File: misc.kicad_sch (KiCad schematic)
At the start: 4 parts, among them J3 PinHeader_2x5_P1.27mm_SMD, U1 MPFS250T-FCVG484, U2 SDINBDG4-8G, U4 MT25QL01GBBB8E_SOP2-16

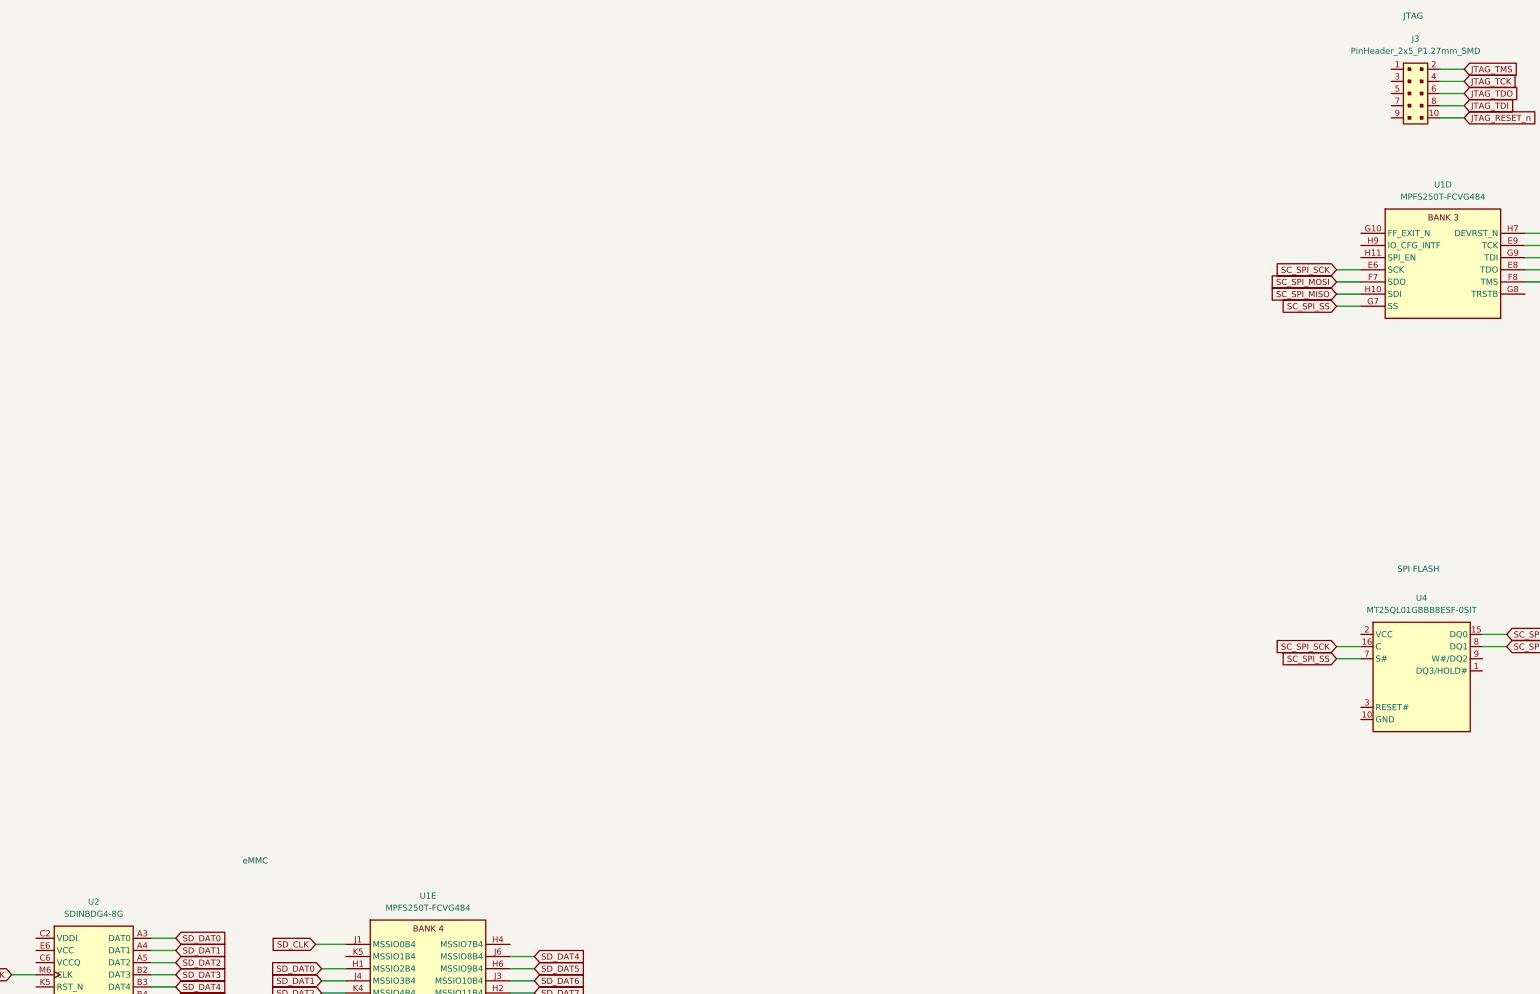
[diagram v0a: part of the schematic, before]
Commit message: [#52577] Clear annotations
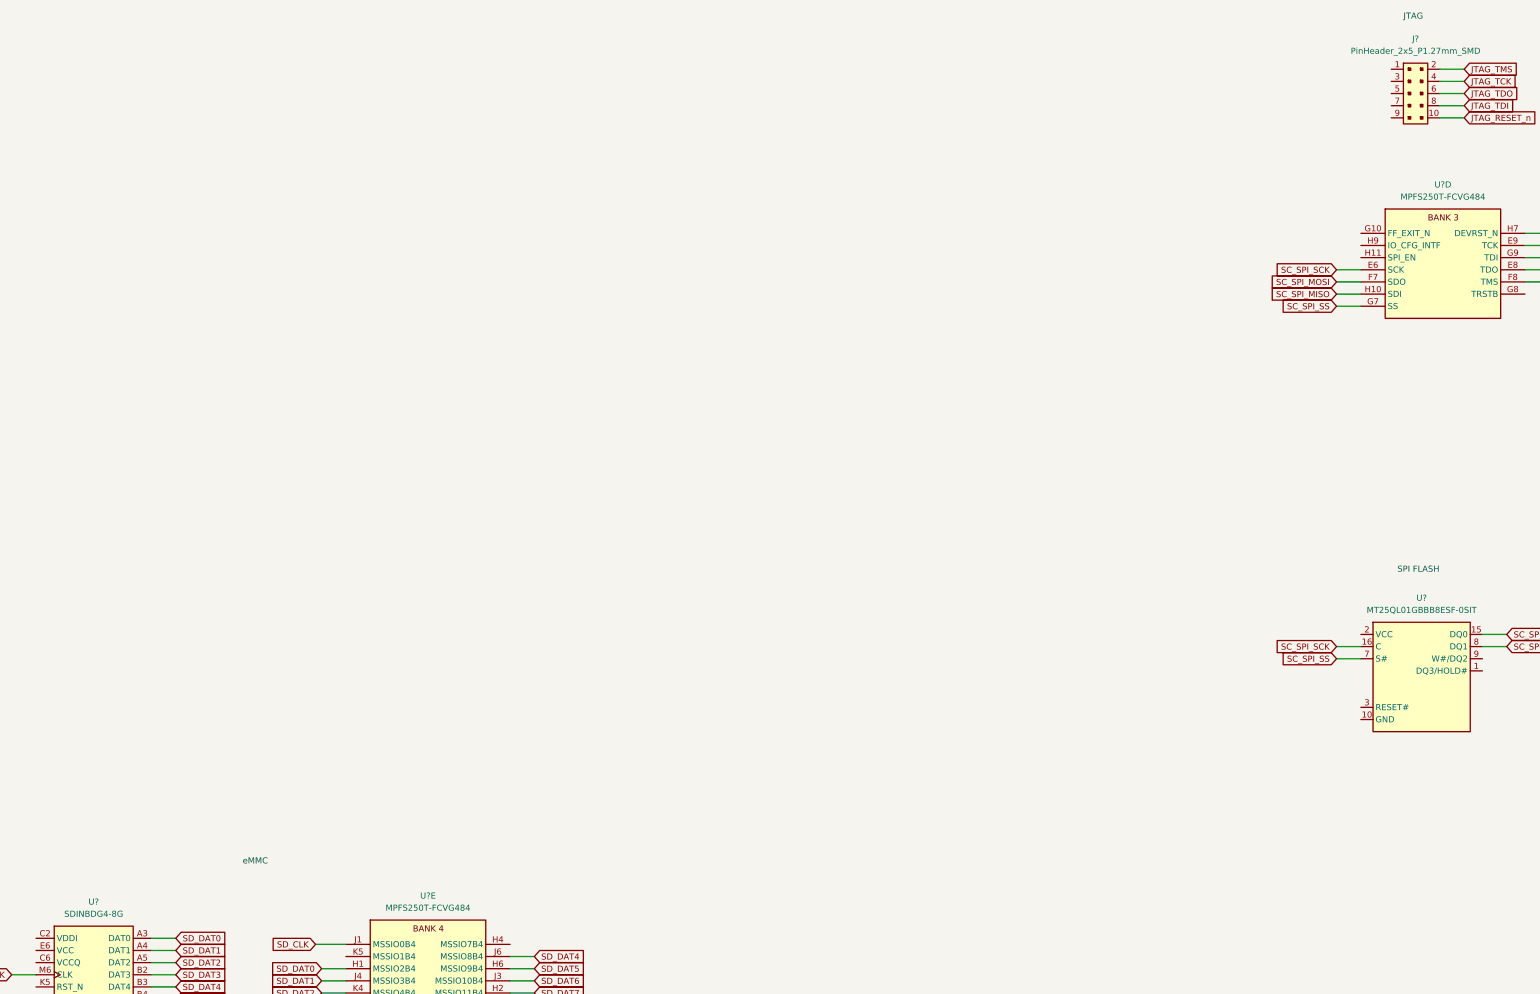
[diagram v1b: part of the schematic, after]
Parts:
- renumbered J3 to J?, U1 to U?, U2 to U?, U4 to U?
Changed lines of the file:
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@@
   (symbol (lib_id "antmicroMicrocontrollers:MPFS250T-FCVG484") (at 116.84 232.41 0) (unit 5)
     (in_bom yes) (on_board yes) (fields_autoplaced)
-    (property "Reference" "U1" (id 0) (at 133.985 222.25 0)
+    (property "Reference" "U?" (id 0) (at 133.985 222.25 0)
       (effects (font (size 1.27 1.27) (thickness 0.15)))
     )
@@
   (symbol (lib_id "antmicroMemory:SDINBDG4-8G") (at 52.07 231.14 0) (unit 1)
     (in_bom yes) (on_board yes) (fields_autoplaced)
-    (property "Reference" "U2" (id 0) (at 64.135 223.52 0)
+    (property "Reference" "U?" (id 0) (at 64.135 223.52 0)
       (effects (font (size 1.27 1.27) (thickness 0.15)))
     )
@@
   (symbol (lib_id "antmicroMemory:MT25QL01GBBB8E_SOP2-16") (at 326.39 167.64 0) (unit 1)
     (in_bom yes) (on_board yes) (fields_autoplaced)
-    (property "Reference" "U4" (id 0) (at 341.63 160.02 0)
+    (property "Reference" "U?" (id 0) (at 341.63 160.02 0)
       (effects (font (size 1.27 1.27) (thickness 0.15)))
     )
@@
   (symbol (lib_id "antmicroMicrocontrollers:MPFS250T-FCVG484") (at 328.93 83.82 0) (unit 4)
     (in_bom yes) (on_board yes) (fields_autoplaced)
-    (property "Reference" "U1" (id 0) (at 346.075 73.66 0)
+    (property "Reference" "U?" (id 0) (at 346.075 73.66 0)
       (effects (font (size 1.27 1.27) (thickness 0.15)))
     )
@@
   (symbol (lib_id "antmicroGenericPinHeaders:PinHeader_2x5_P1.27mm_SMD") (at 335.28 49.53 0) (unit 1)
     (in_bom yes) (on_board yes) (fields_autoplaced)
-    (property "Reference" "J3" (id 0) (at 340.36 43.18 0)
+    (property "Reference" "J?" (id 0) (at 340.36 43.18 0)
       (effects (font (size 1.27 1.27) (thickness 0.15)))
     )

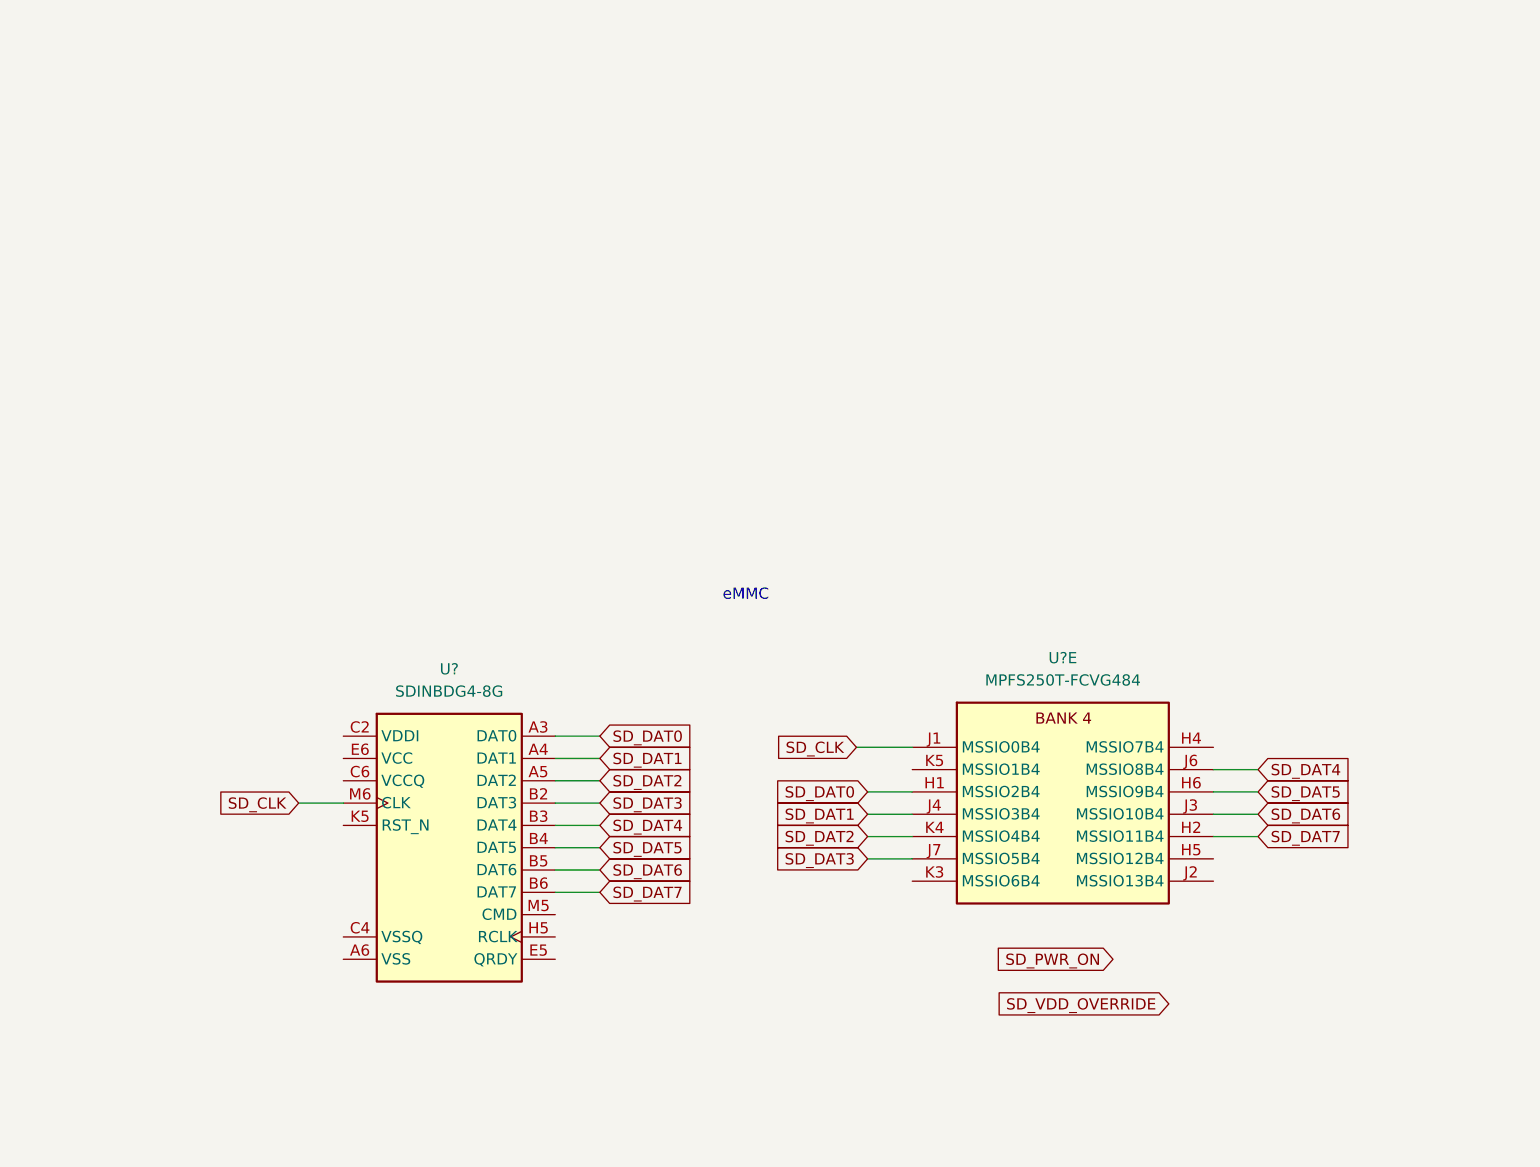
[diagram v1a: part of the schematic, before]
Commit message: [#54013] Add resistor array
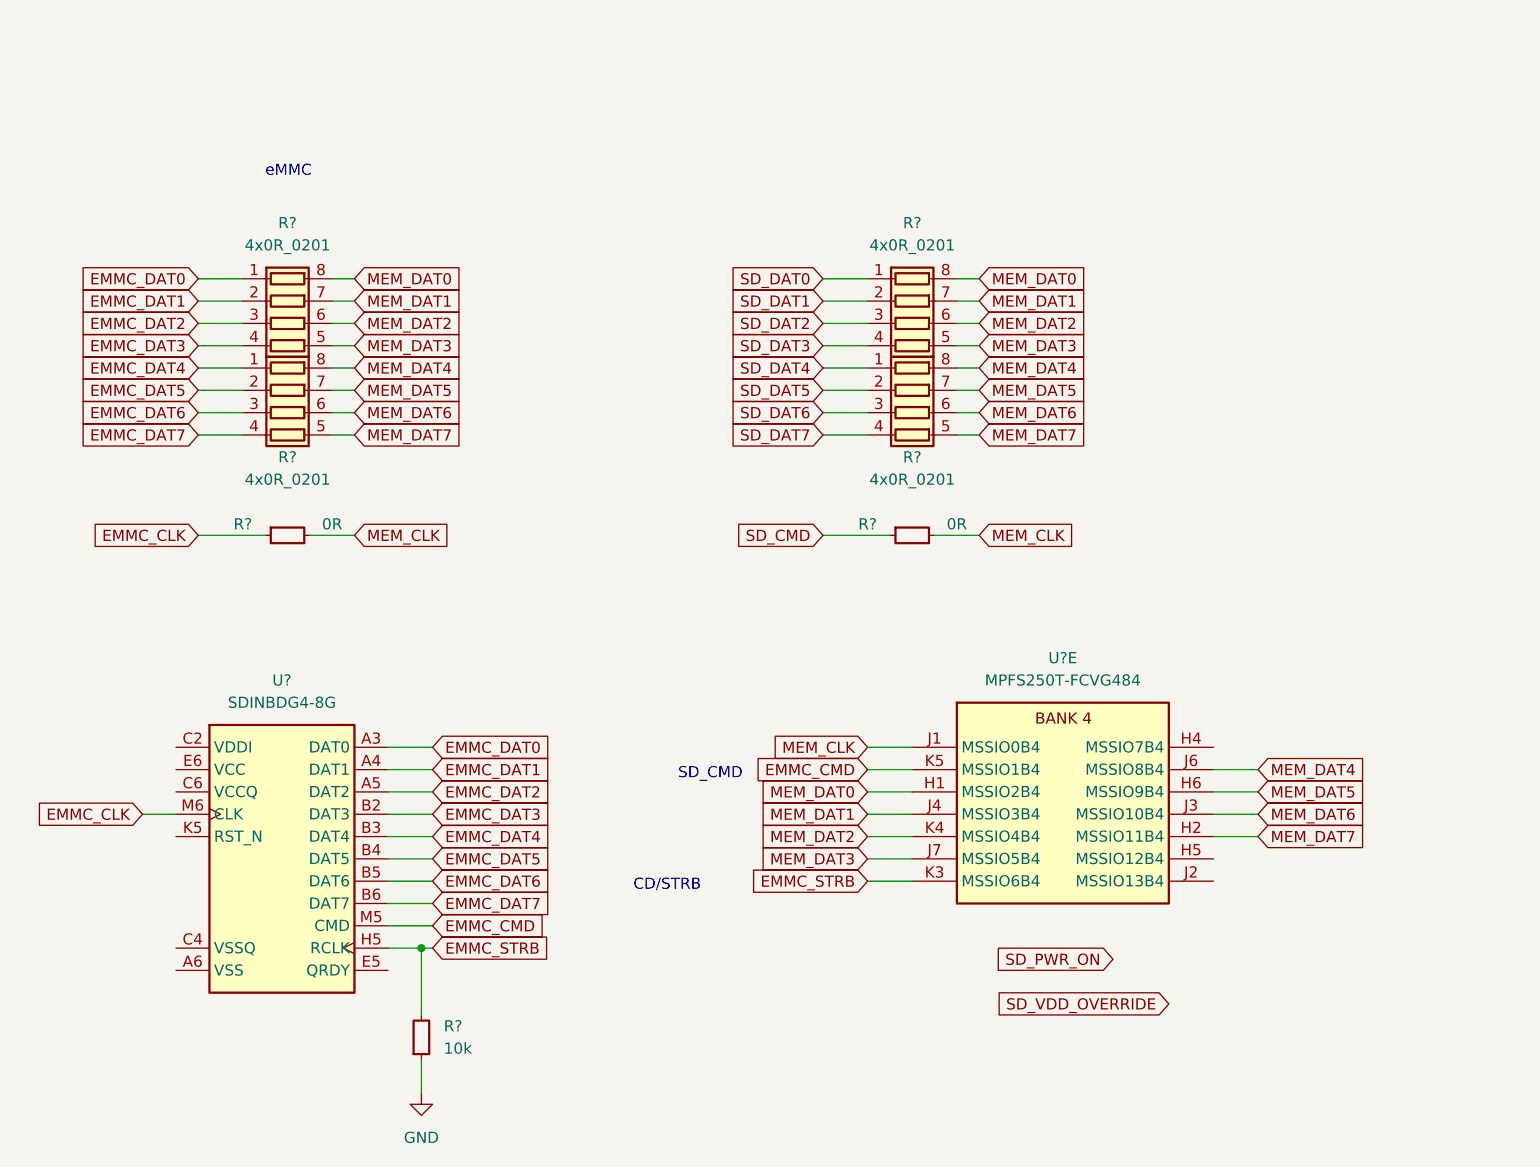
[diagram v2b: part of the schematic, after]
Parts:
- added R? (x4): R_4x0R_0201_array, antmicro-footprints:R_Array_4x0201_Panasonic_EXB18V, symbol antmicroResistorNetworksArrays:R_4x0R_0201_array
- added R?: R_10k_0402, antmicro-footprints:R_0402_1005Metric, symbol antmicroResistors0402:R_10k_0402
- added R? (x2): R_0R_0402, antmicro-footprints:R_0402_1005Metric, symbol antmicroResistors0402:R_0R_0402
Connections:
- net SD_DAT0: now also R?.1 (R1.1); no longer U?.A3 (DAT0), U?.H1 (MSSIO2B4)
- net SD_DAT1: now also R?.2 (R2.1); no longer U?.A4 (DAT1), U?.J4 (MSSIO3B4)
- net SD_DAT2: now also R?.3 (R3.1); no longer U?.A5 (DAT2), U?.K4 (MSSIO4B4)
- net SD_DAT3: now also R?.4 (R4.1); no longer U?.B2 (DAT3), U?.J7 (MSSIO5B4)
- net SD_DAT4: now also R?.1 (R1.1); no longer U?.B3 (DAT4), U?.J6 (MSSIO8B4)
- net SD_DAT5: now also R?.2 (R2.1); no longer U?.B4 (DAT5), U?.H6 (MSSIO9B4)
- net SD_DAT6: now also R?.3 (R3.1); no longer U?.B5 (DAT6), U?.J3 (MSSIO10B4)
- net SD_DAT7: now also R?.4 (R4.1); no longer U?.B6 (DAT7), U?.H2 (MSSIO11B4)
- net EMMC_STRB: now reaches U?.K3 (MSSIO6B4)
- net EMMC_STRB: now also U?.H5 (RCLK), R?.2
- net EMMC_CMD: now reaches U?.K5 (MSSIO1B4)
- net EMMC_CMD: now also U?.M5 (CMD)
- net SD_CLK renamed EMMC_CLK
- net EMMC_CLK: now also R?.1; no longer U?.J1 (MSSIO0B4)
- new net EMMC_DAT0: R?.1 (R1.1), U?.A3 (DAT0)
- new net EMMC_DAT1: R?.2 (R2.1), U?.A4 (DAT1)
- new net EMMC_DAT2: R?.3 (R3.1), U?.A5 (DAT2)
- new net EMMC_DAT3: R?.4 (R4.1), U?.B2 (DAT3)
- new net EMMC_DAT4: R?.1 (R1.1), U?.B3 (DAT4)
- new net EMMC_DAT5: R?.2 (R2.1), U?.B4 (DAT5)
- new net EMMC_DAT6: R?.3 (R3.1), U?.B5 (DAT6)
- new net EMMC_DAT7: R?.4 (R4.1), U?.B6 (DAT7)
- new net GND: R?.1
- new net MEM_CLK: R?.2, R?.2, U?.J1 (MSSIO0B4)
- new net MEM_DAT0: R?.8 (R1.2), R?.8 (R1.2), U?.H1 (MSSIO2B4)
- new net MEM_DAT1: R?.7 (R2.2), R?.7 (R2.2), U?.J4 (MSSIO3B4)
- new net MEM_DAT2: R?.6 (R3.2), R?.6 (R3.2), U?.K4 (MSSIO4B4)
- new net MEM_DAT3: R?.5 (R4.2), R?.5 (R4.2), U?.J7 (MSSIO5B4)
- new net MEM_DAT4: R?.8 (R1.2), R?.8 (R1.2), U?.J6 (MSSIO8B4)
- new net MEM_DAT5: R?.7 (R2.2), R?.7 (R2.2), U?.H6 (MSSIO9B4)
- new net MEM_DAT6: R?.6 (R3.2), R?.6 (R3.2), U?.J3 (MSSIO10B4)
- new net MEM_DAT7: R?.5 (R4.2), R?.5 (R4.2), U?.H2 (MSSIO11B4)
- new net SD_CMD: R?.1
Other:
- note added: "CD/STRB"
- note added: "SD_CMD"
- moved on the sheet: U?
